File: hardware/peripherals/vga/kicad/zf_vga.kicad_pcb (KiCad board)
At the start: 2 copper layers, 143 x 85 mm, 52 parts, among them J2 Z-FIGHTER Expansion Port, J3 DB15_Female, J4 DB9_Male, J5 DB9_Male, SW1 SW_DIP_x03, U1 4040, U10 74HC165, U11 AS6C6264, U12 74HC541, U13 74HC541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

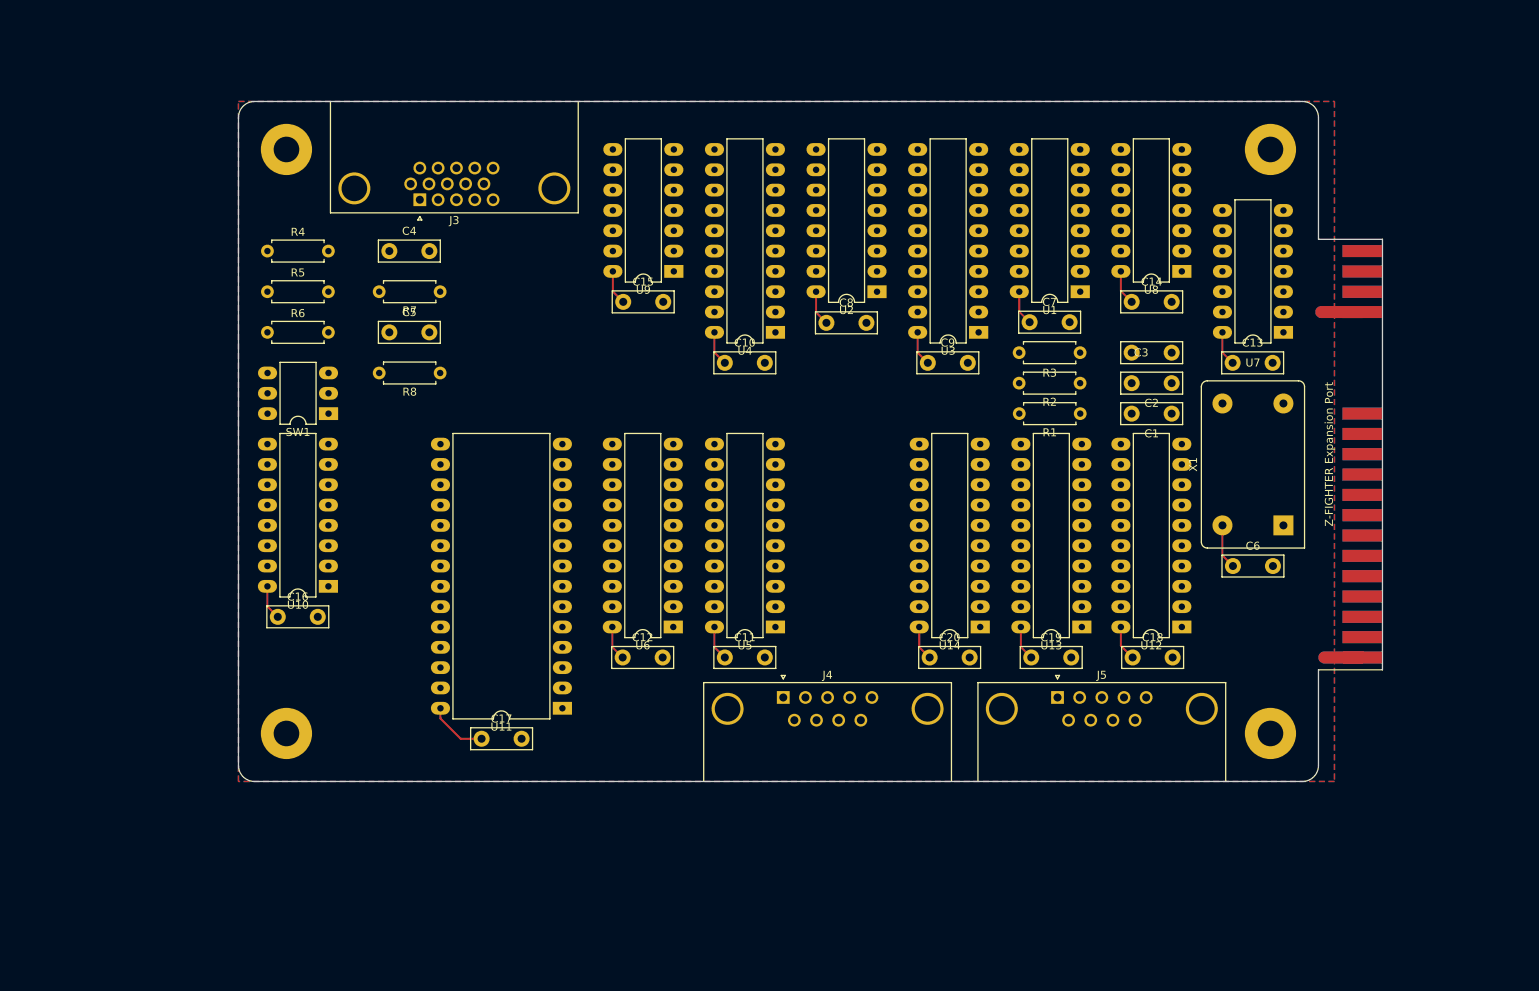
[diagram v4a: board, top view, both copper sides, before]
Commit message: Routing draft, changed SRAM NC pin to VCC
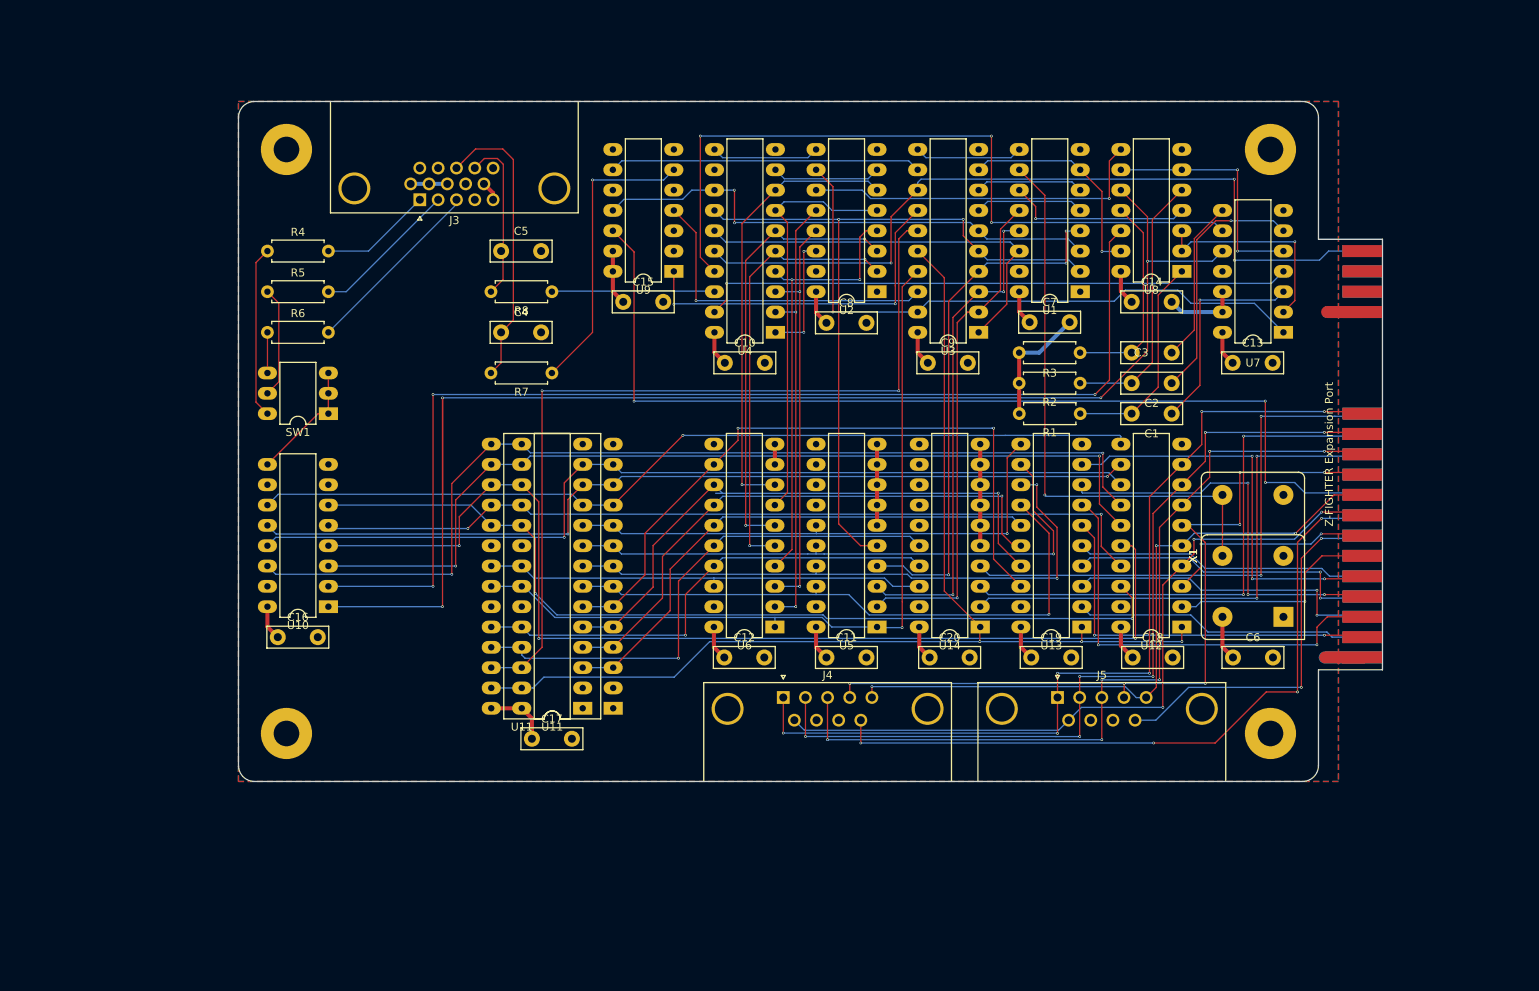
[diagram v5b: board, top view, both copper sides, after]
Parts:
- added U11: AS6C6264, Package_DIP:DIP-28_W7.62mm_LongPads, F.Cu at (129.6, 100.3)
- added X1: CXO_DIP14, Oscillator:Oscillator_DIP-8_LargePads, F.Cu at (217.2, 88.9)
- moved R7 17.3 mm to (125.8, 58.4)
- moved R8 17.3 mm to (125.8, 48.3)
- moved C4 17.3 mm to (119.4, 53.4)
- moved C5 17.3 mm to (119.4, 43.2)
- moved C11 12.7 mm to (160.1, 94.0)
- moved U5 12.7 mm to (166.4, 90.2)
- moved C12 12.7 mm to (147.3, 94.0)
- moved U6 12.7 mm to (153.7, 90.2)
- moved C6 11.4 mm to (210.9, 94.0)
- moved X1 11.4 mm to (217.2, 88.9)
- moved U11 6.35 mm to (133.5, 100.3)
- moved C17 6.29 mm to (123.3, 104.2)
- moved U10 2.54 mm to (97.9, 87.6)
- moved C16 2.54 mm to (91.5, 91.5)
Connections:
- U11 pad 1: Net-(U11-Pad1) -> VCC
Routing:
- net #LDPULSE: track 0.00 -> 175.4 mm, vias 0 -> 4
- net #WE: track 0.00 -> 144.5 mm, vias 0 -> 3
- net #P1: track 0.00 -> 141.6 mm, vias 0 -> 3
- net D5: track 0.00 -> 137.3 mm, vias 0 -> 3
- net D3: track 0.00 -> 126.1 mm, vias 0 -> 2
- net DATARDY: track 0.00 -> 124.3 mm, vias 0 -> 3
- net D4: track 0.00 -> 116.7 mm, vias 0 -> 2
- net D2: track 0.00 -> 115.9 mm, vias 0 -> 1
- net D7: track 0.00 -> 115.0 mm, vias 0 -> 2
- net D1: track 0.00 -> 113.3 mm, vias 0 -> 2
- net D0: track 0.00 -> 112.4 mm, vias 0 -> 1
- net PA0: track 0.00 -> 111.5 mm, vias 0 -> 6
- net PA1: track 0.00 -> 108.8 mm, vias 0 -> 6
- net D6: track 0.00 -> 106.0 mm, vias 0 -> 2
- net CE2: track 0.00 -> 105.8 mm, vias 0 -> 2
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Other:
- net class Default: clearance 0.2 -> 0.1524; trace_width 0.25 -> 0.1524; via_dia 0.8 -> 0.3302; via_drill 0.4 -> 0.2
- net class Power added: clearance 0.1524, trace_width 0.508, via_dia 0.8, via_drill 0.2
- rule trace_clearance: 0.2 -> 0.1524
- rule trace_min: 0.2 -> 0.1524
- rule via_min_drill: 0.3 -> 0.2
- rule via_min_size: 0.4 -> 0.3302

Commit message: Routing progress
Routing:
- net #LDPULSE: track 175.4 -> 162.3 mm
- net GND: track 68.1 -> 55.4 mm
- net PC5: track 88.1 -> 92.2 mm, vias 4 -> 5
- net PC6: track 47.4 -> 49.4 mm, vias 2 -> 3
- net PA2: track 104.6 -> 105.9 mm
- net PA3: track 98.6 -> 97.5 mm
- net PC0: track 68.2 -> 67.3 mm

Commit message: Routing, silkscreen
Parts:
- added G***: LOGO, zf_vga:Tangent_Head, B.Cu at (107.4, 98.8)
- added G***: LOGO, zf_vga:Z-FIGHTER_Logo, F.Cu at (108.5, 48.3)
- Joystick 1: renamed from J4
- Joystick 2: renamed from J5
- VGA Output: renamed from J3
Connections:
- U11 pad 1: VCC -> GND (x2)
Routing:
- net GND: track 55.4 -> 35.1 mm
- net PA3: track 97.5 -> 101.5 mm, vias 6 -> 5
- net P4: track 65.0 -> 62.6 mm, vias 2 -> 0
- net PA2: track 105.9 -> 108.2 mm, vias 6 -> 5
- net CLOCK: track 71.9 -> 73.8 mm, vias 1 -> 2
- net L8: track 55.7 -> 54.2 mm, vias 2 -> 1
- net VIDOUT: track 15.3 -> 16.4 mm
- net PC6: track 49.4 -> 50.5 mm
- net P6: track 66.0 -> 65.1 mm, vias 3 -> 2
- net L9: track 15.2 -> 14.3 mm, vias 2 -> 1
- net A5: track 73.9 -> 73.1 mm
- net A4: track 85.7 -> 86.5 mm
- net P8: track 62.9 -> 62.1 mm
- net D5: track 137.3 -> 136.5 mm
- net CE2: track 105.8 -> 105.1 mm
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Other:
- net class Default: via_dia 0.3302 -> 0.6; via_drill 0.2 -> 0.3
- board text added: "Z-FIGHTER VGA Module Rev. 0 @tangent3D 2022"

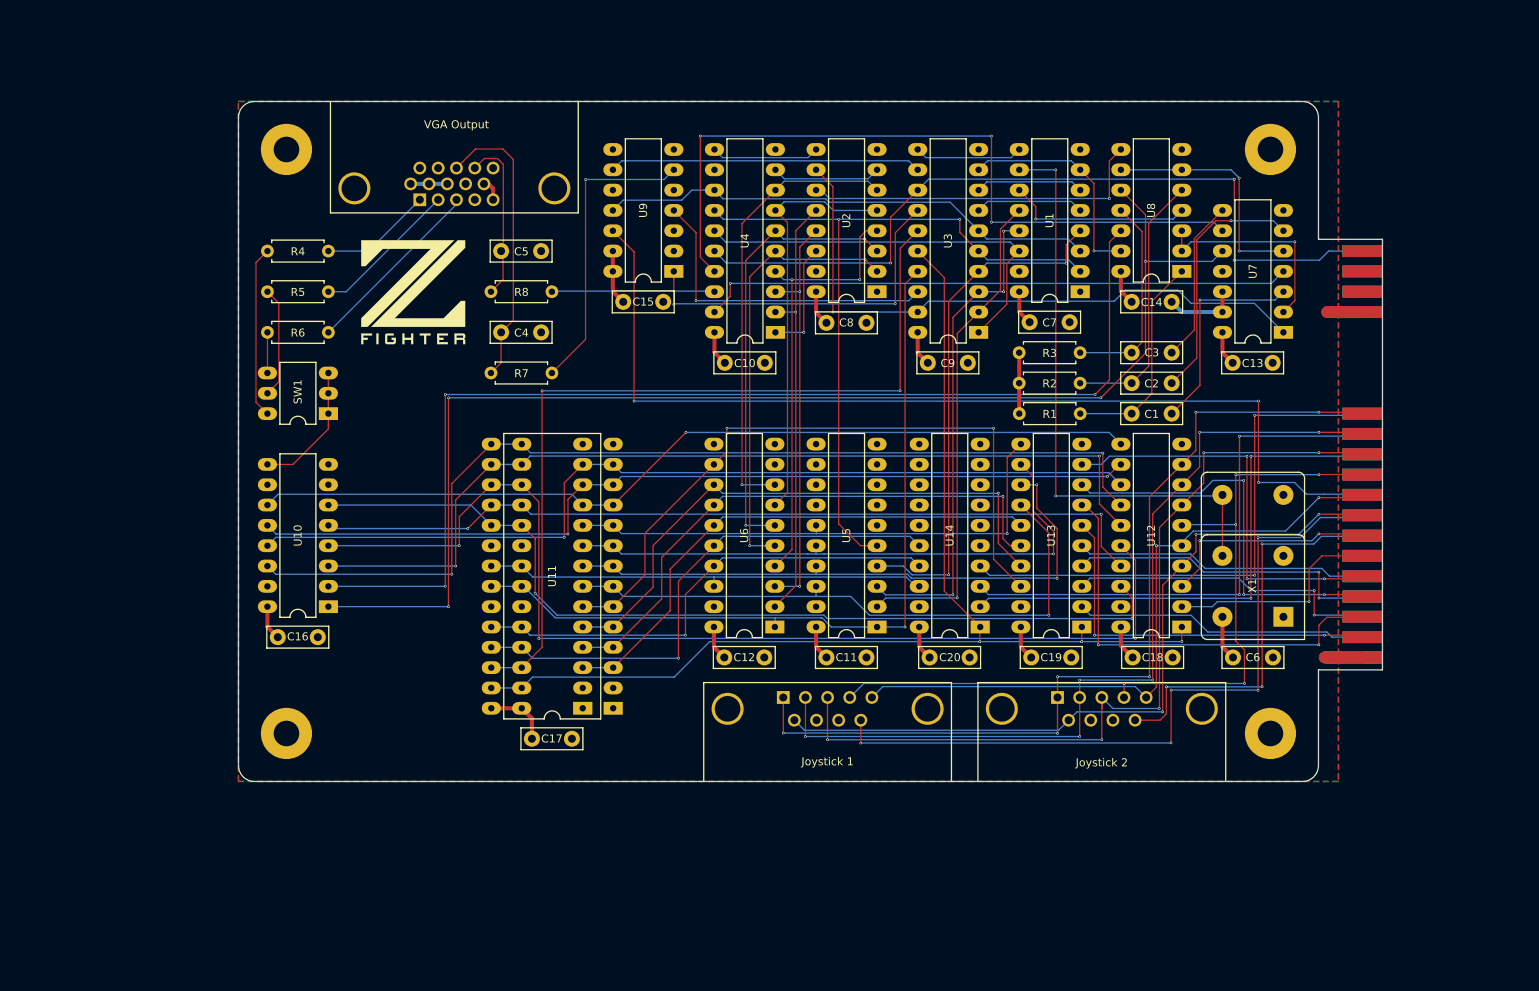
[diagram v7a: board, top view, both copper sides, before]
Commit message: Progress switching to 0.3mm via drill, 0.6mm via size
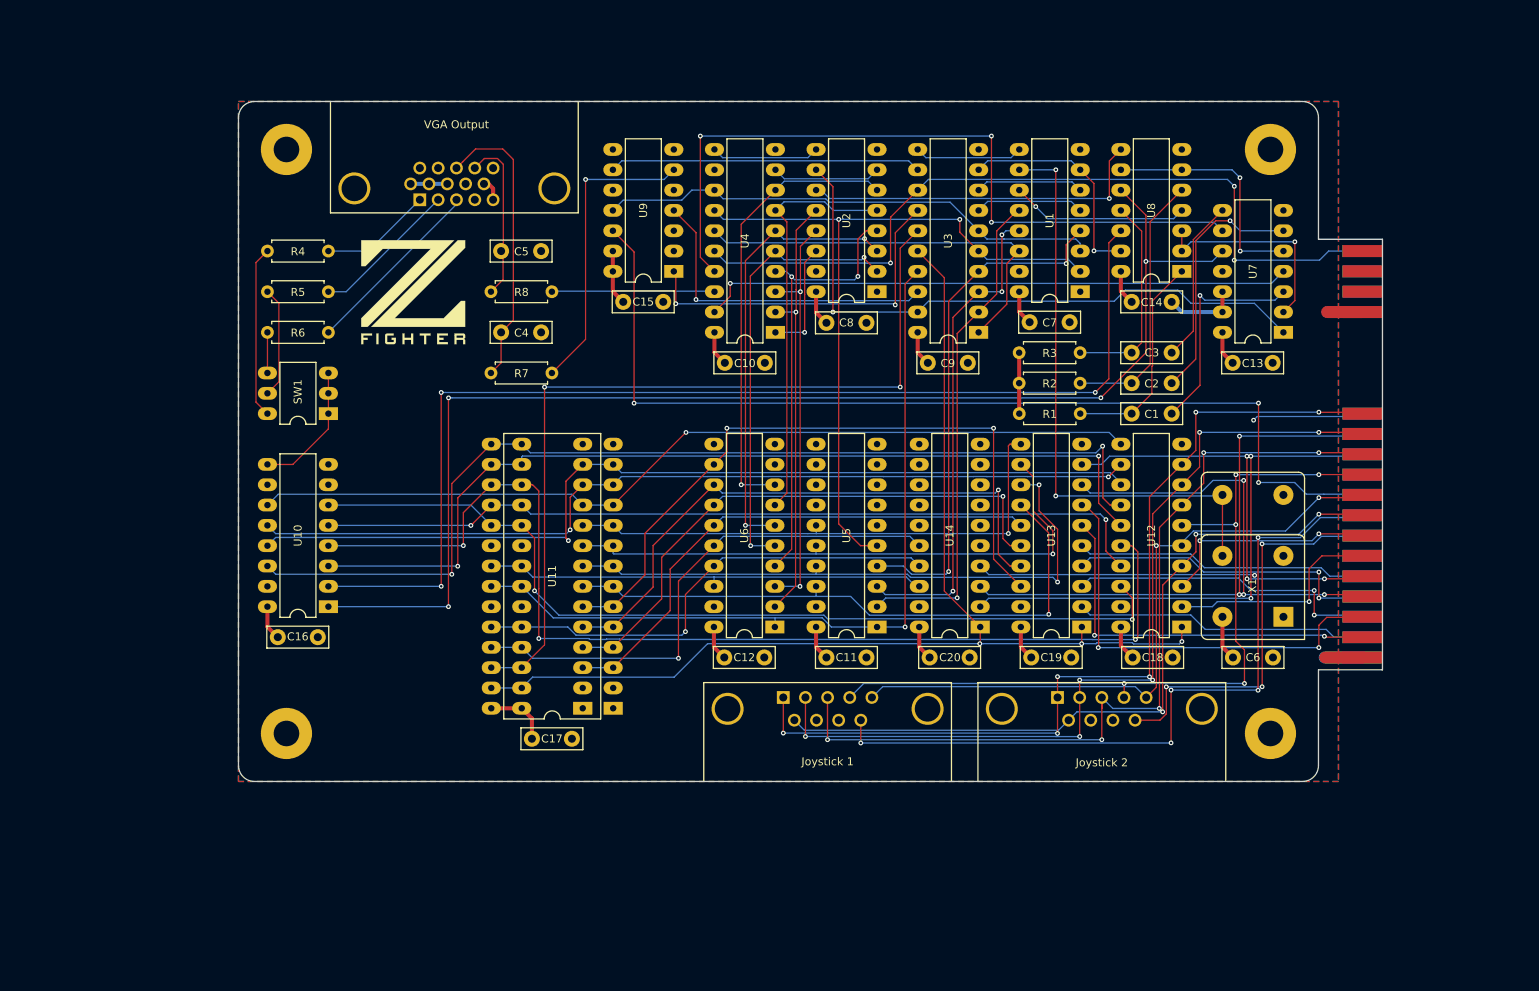
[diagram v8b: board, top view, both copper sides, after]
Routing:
- net PC0: track 67.3 -> 47.8 mm
- net D5: track 136.5 -> 138.8 mm
- net D3: track 126.1 -> 128.1 mm
- net A5: track 73.1 -> 74.4 mm
- net D2: track 115.9 -> 117.2 mm
- net PRESET: track 23.2 -> 22.2 mm
- net A2: track 75.8 -> 76.7 mm
- net A0: track 66.4 -> 67.3 mm
- net Net-(C1-Pad1): track 26.5 -> 27.3 mm
- net PB2: track 54.0 -> 54.7 mm
- net D4: track 116.7 -> 117.4 mm
- net #WE: track 144.5 -> 145.1 mm
- net P4: track 62.6 -> 63.2 mm
- net #RESET: track 100.0 -> 99.5 mm
